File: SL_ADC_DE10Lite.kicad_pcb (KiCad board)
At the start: 4 copper layers, 24 parts, among them J1 Conn_02x20_Odd_Even, J2 Conn_02x08_Odd_Even, J3 Conn_02x05_Counter_Clockwise, J5 Conn_02x07_Counter_Clockwise

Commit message: Update net names
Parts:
- moved J1 8.45 mm to (181.5, 75.5)
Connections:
- net /GPIO(23)-REFIN/~{WR} renamed /GPIO(23)-REFEN/~{WR}
- IC1 pad 36: /DGND -> /ASLEEP
- IC1 pad 63: /REFCP -> /CH_C1
- J1 pad 21: unconnected-(J1-Pin_21-Pad21) -> /ASLEEP
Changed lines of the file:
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@@
 		(capping no)
 		(filling no)
-		(zone_defaults)
 		(pcbplotparams
 			(layerselection 0x00000000_00000000_55555555_5755f5ff)
@@
 			(layers "F.Cu" "F.Mask" "F.Paste")
 			(roundrect_rratio 0.25)
-			(net "/GPIO(23)-REFIN{slash}~{WR}")
+			(net "/GPIO(23)-REFEN{slash}~{WR}")
 			(pinfunction "REFEN/~{WR}_11")
 			(pintype "input")
@@
 			(layers "F.Cu" "F.Mask" "F.Paste")
 			(roundrect_rratio 0.25)
-			(net "/DGND")
+			(net "/ASLEEP")
 			(pinfunction "ASLEEP_36")
 			(pintype "input")
@@
 			(layers "F.Cu" "F.Mask" "F.Paste")
 			(roundrect_rratio 0.25)
-			(net "/REFCP")
+			(net "/CH_C1")
 			(pinfunction "REFCP_63")
 			(pintype "input")
@@
 	(footprint "Connector_PinSocket_2.54mm:PinSocket_2x20_P2.54mm_Vertical"
 		(layer "B.Cu")
-		(at 178.46 83.36 180)
+		(at 181.46 75.46 180)
 		(descr "Through hole straight socket strip, 2x20, 2.54mm pitch, double rows (from Kicad 4.0.7), script generated")
 		(tags "Through hole socket strip THT 2x20 2.54mm double row")
@@
 			(layers "*.Cu" "*.Mask")
 			(remove_unused_layers no)
-			(net "unconnected-(J1-Pin_21-Pad21)")
+			(net "/ASLEEP")
 			(pinfunction "Pin_21_21")
-			(pintype "passive+no_connect")
+			(pintype "passive")
 		)
 		(pad "22" thru_hole circle
@@
 			(layers "*.Cu" "*.Mask")
 			(remove_unused_layers no)
-			(net "/GPIO(23)-REFIN{slash}~{WR}")
+			(net "/GPIO(23)-REFEN{slash}~{WR}")
 			(pinfunction "Pin_26_26")
 			(pintype "passive")
@@
 	)
 	(segment
+		(start 140.5375 96)
+		(end 137.75 98.7875)
+		(width 0.2)
+		(layer "F.Cu")
+		(net "/REFBP")
+	)
+	(segment
+		(start 137.75 98.7875)
+		(end 137.75 104.3375)
+		(width 0.2)
+		(layer "F.Cu")
+		(net "/REFBP")
+	)
+	(segment
+		(start 140.5375 95.5375)
+		(end 140.5 95.5)
+		(width 0.2)
+		(layer "F.Cu")
+		(net "/REFBP")
+	)
+	(segment
+		(start 140.5375 96)
+		(end 140.5375 95.5375)
+		(width 0.2)
+		(layer "F.Cu")
+		(net "/REFBP")
+	)
+	(segment
 		(start 136.0375 96)
 		(end 135.25 96.7875)
@@
 		(net "/REFCP")
 	)
-	(segment
-		(start 140.5375 96)
-		(end 137.75 98.7875)
-		(width 0.2)
-		(layer "F.Cu")
-		(net "/REFBP")
-	)
-	(segment
-		(start 137.75 98.7875)
-		(end 137.75 104.3375)
-		(width 0.2)
-		(layer "F.Cu")
-		(net "/REFBP")
-	)
-	(segment
-		(start 140.5375 95.5375)
-		(end 140.5 95.5)
-		(width 0.2)
-		(layer "F.Cu")
-		(net "/REFBP")
-	)
-	(segment
-		(start 140.5375 96)
-		(end 140.5375 95.5375)
-		(width 0.2)
-		(layer "F.Cu")
-		(net "/REFBP")
-	)
 	(embedded_fonts no)

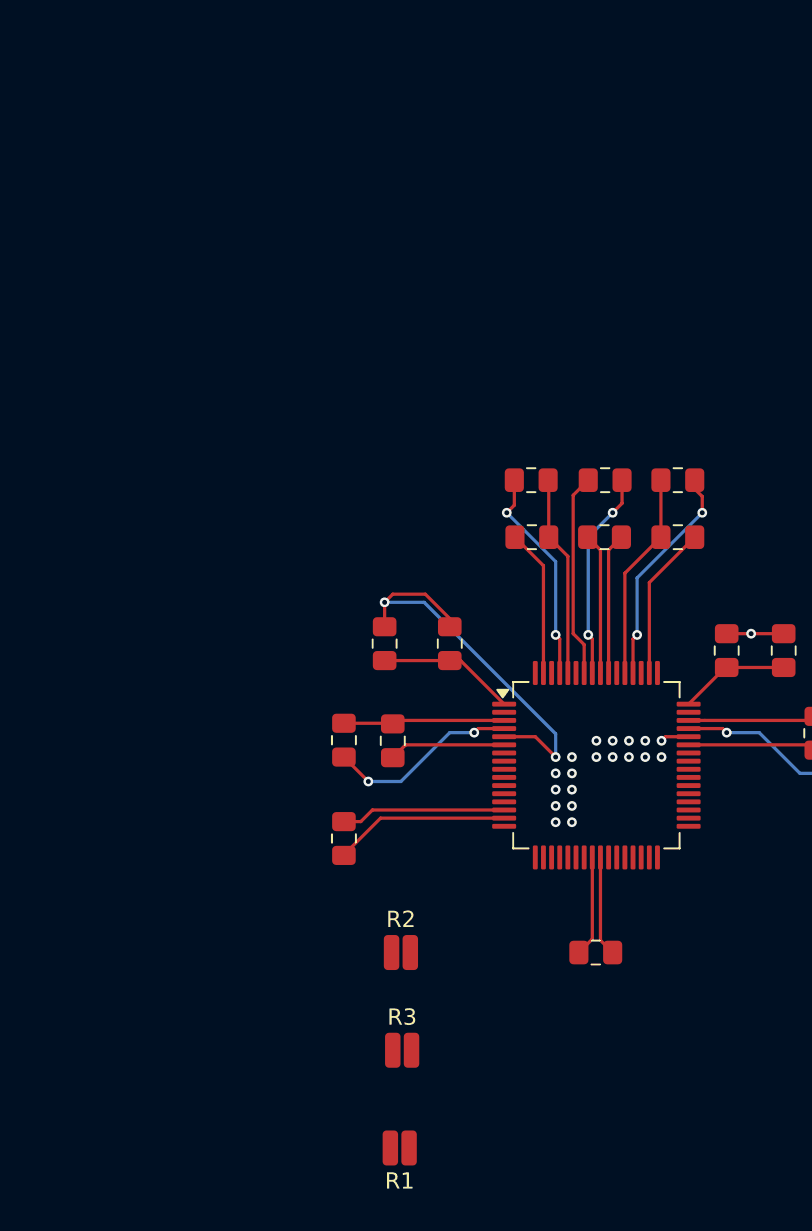
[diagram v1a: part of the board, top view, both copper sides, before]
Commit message: Add analog header
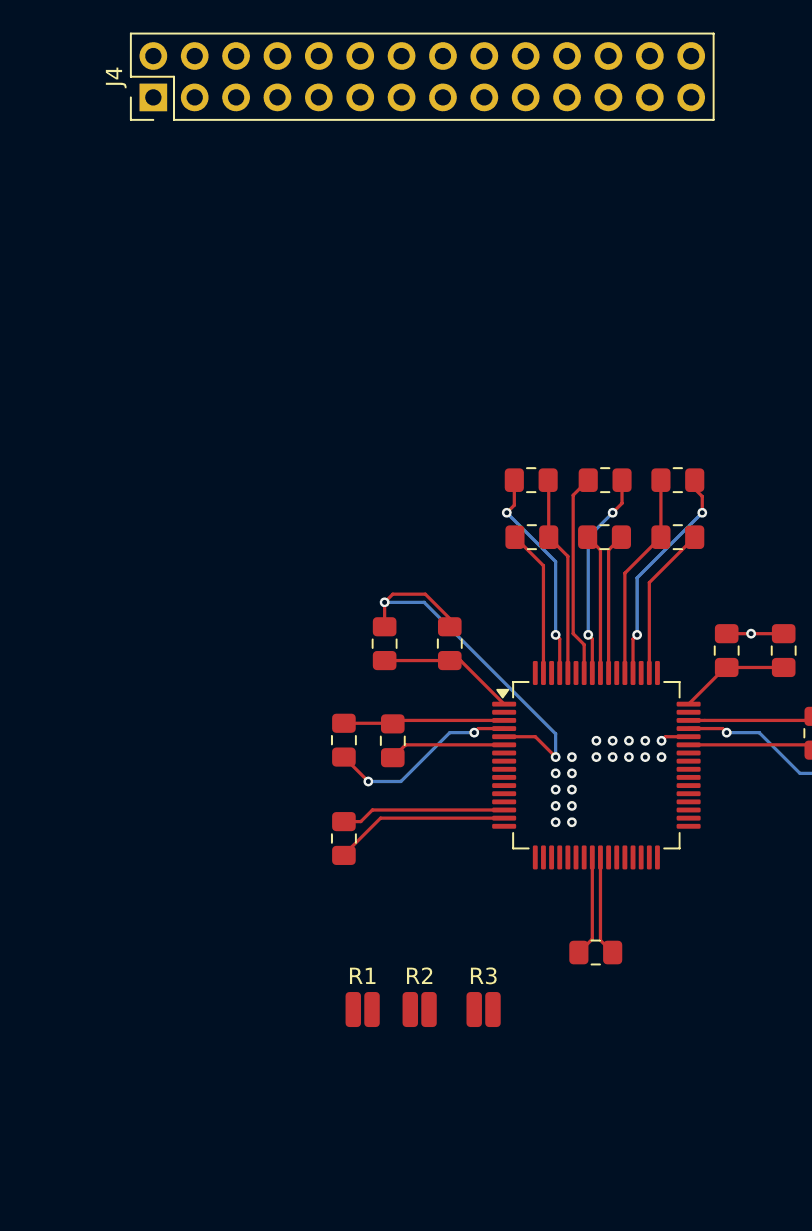
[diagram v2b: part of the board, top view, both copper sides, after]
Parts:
- added J4: Analog header, Connector_PinHeader_2.54mm:PinHeader_2x14_P2.54mm_Vertical, F.Cu at (107.3, 69.0)
- J1: value Conn_02x20_Odd_Even -> DE10Lite header
- J3: value Conn_02x05_Counter_Clockwise -> Digital ground header
- J5: value Conn_02x07_Counter_Clockwise -> Power header
- moved R1 8.80 mm to (120.2, 125.0), turned to 0 degrees
- moved R3 5.59 mm to (127.6, 125.0)
- moved R2 3.68 mm to (123.7, 125.0)
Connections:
- IC1 pad 63: /CH_C1 -> /REFCP

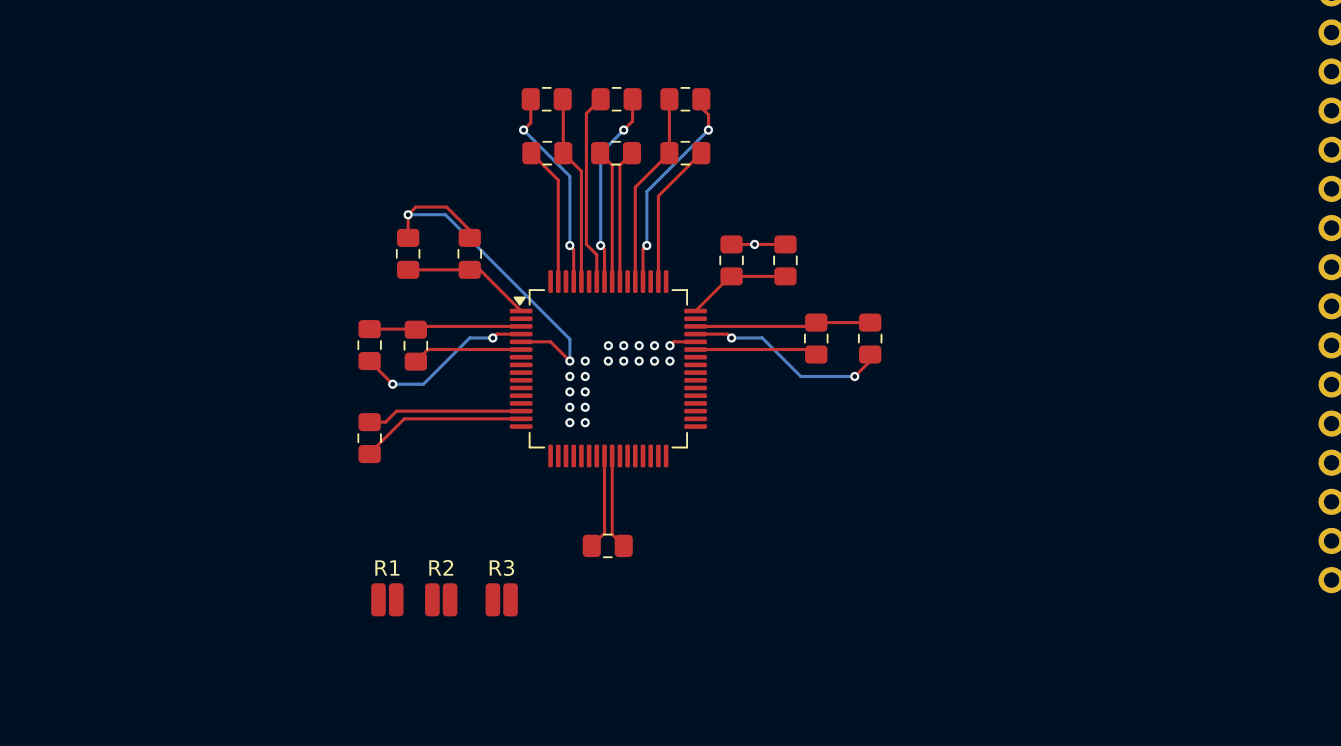
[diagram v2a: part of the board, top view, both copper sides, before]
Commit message: left feedback for first run of work as comments and silkscreen labels. To be deleted
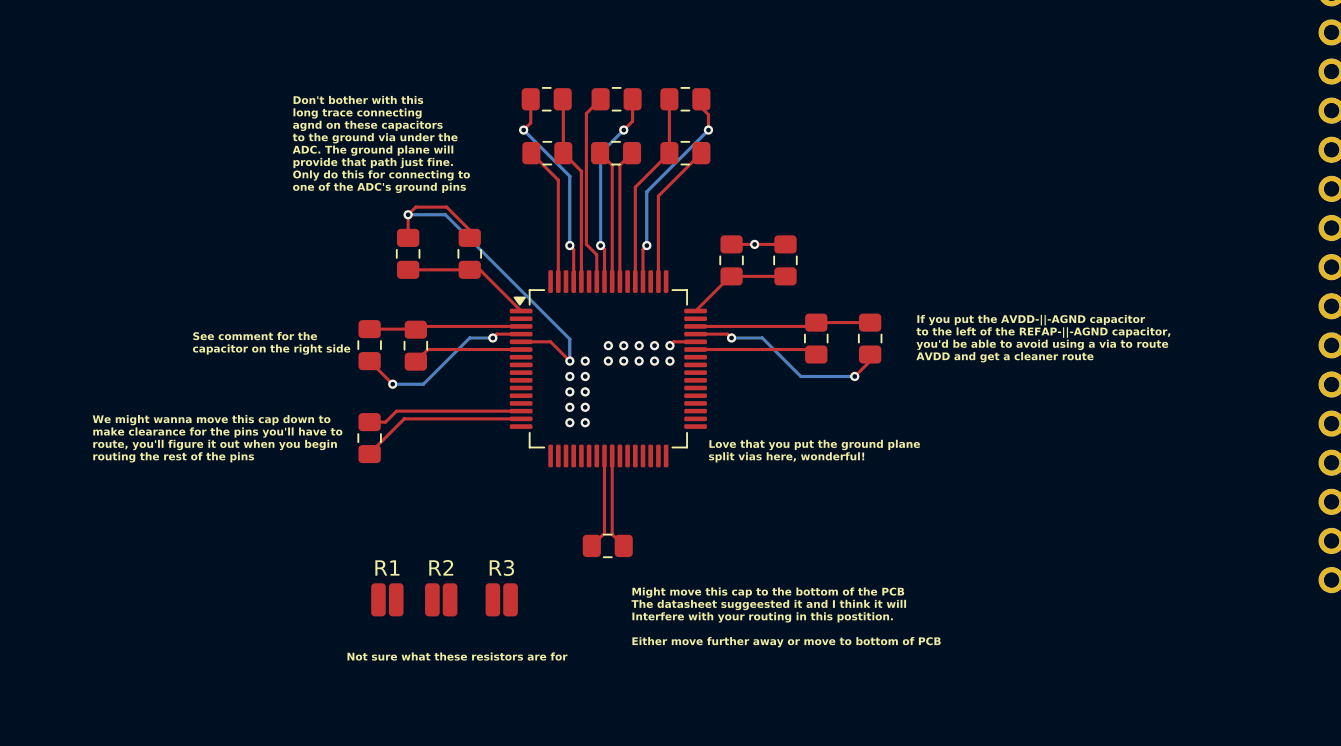
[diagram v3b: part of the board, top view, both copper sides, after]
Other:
- board text added: "Don't bother with this long trace connecting agnd on these capacitors to the ground via under the ADC. The ground plane will provide that path just fine. Only do this for connecting to one of the ADC's ground pins"
- board text added: "If you put the AVDD-||-AGND capacitor to the left of the REFAP-||-AGND capacitor, you'd be able to avoid using a via to route AVDD and get a cleaner route"
- board text added: "Love that you put the ground plane split vias here, wonderful!"
- board text added: "Might move this cap to the bottom of the PCB The datasheet suggeested it and I think it will Interfere with your routing in this postition. Either move further away or move to bottom of PCB"
- board text added: "Not sure what these resistors are for"
- board text added: "See comment for the capacitor on the right side"
- board text added: "We might wanna move this cap down to make clearance for the pins you'll have to route, you'll figure it out when you begin routing the rest of the pins"
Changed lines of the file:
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@@
+		)
+	)
+	(gr_text "We might wanna move this cap down to\nmake clearance for the pins you'll have to \nroute, you'll figure it out when you begin\nrouting the rest of the pins"
+		(at 101 116 0)
+		(layer "F.SilkS")
+		(effects
+			(font
+				(size 0.5 0.5)
+				(thickness 0.125)
+				(bold yes)
+			)
+			(justify left bottom)
+		)
+	)
+	(gr_text "See comment for the\ncapacitor on the right side"
+		(at 107.5 109 0)
+		(layer "F.SilkS")
+		(effects
+			(font
+				(size 0.5 0.5)
+				(thickness 0.125)
+				(bold yes)
+			)
+			(justify left bottom)
+		)
+	)
+	(gr_text "Don't bother with this\nlong trace connecting\nagnd on these capacitors\nto the ground via under the\nADC. The ground plane will\nprovide that path just fine.\nOnly do this for connecting to \none of the ADC's ground pins"
+		(at 114 98.5 0)
+		(layer "F.SilkS")
+		(effects
+			(font
+				(size 0.5 0.5)
+				(thickness 0.125)
+				(bold yes)
+			)
+			(justify left bottom)
+		)
+	)
+	(gr_text "Not sure what these resistors are for"
+		(at 117.5 129 0)
+		(layer "F.SilkS")
+		(effects
+			(font
+				(size 0.5 0.5)
+				(thickness 0.125)
+				(bold yes)
+			)
+			(justify left bottom)
+		)
+	)
+	(gr_text "Might move this cap to the bottom of the PCB\nThe datasheet suggeested it and I think it will \nInterfere with your routing in this postition.\n\nEither move further away or move to bottom of PCB"
+		(at 136 128 0)
+		(layer "F.SilkS")
+		(effects
+			(font
+				(size 0.5 0.5)
+				(thickness 0.125)
+				(bold yes)
+			)
+			(justify left bottom)
+		)
+	)
+	(gr_text "Love that you put the ground plane\nsplit vias here, wonderful!\n"
+		(at 141 116 0)
+		(layer "F.SilkS")
+		(effects
+			(font
+				(size 0.5 0.5)
+				(thickness 0.125)
+				(bold yes)
+			)
+			(justify left bottom)
+		)
+	)
+	(gr_text "If you put the AVDD-||-AGND capacitor\nto the left of the REFAP-||-AGND capacitor, \nyou'd be able to avoid using a via to route \nAVDD and get a cleaner route"
+		(at 154.5 109.5 0)
+		(layer "F.SilkS")
+		(effects
+			(font
+				(size 0.5 0.5)
+				(thickness 0.125)
+				(bold yes)
+			)
+			(justify left bottom)
 		)
 	)
